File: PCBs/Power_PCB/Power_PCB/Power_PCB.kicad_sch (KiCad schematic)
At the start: 8 parts, among them IC1 ADS1115BQDGSRQ1, IC2 ADS1115BQDGSRQ1, IC3 ACS712ELCTR-20A-T, J1 XT60PW-F, J2 XT60PW-F, J3 XT60PW-F, J4 XT60PW-F, U1 ESP32-S3

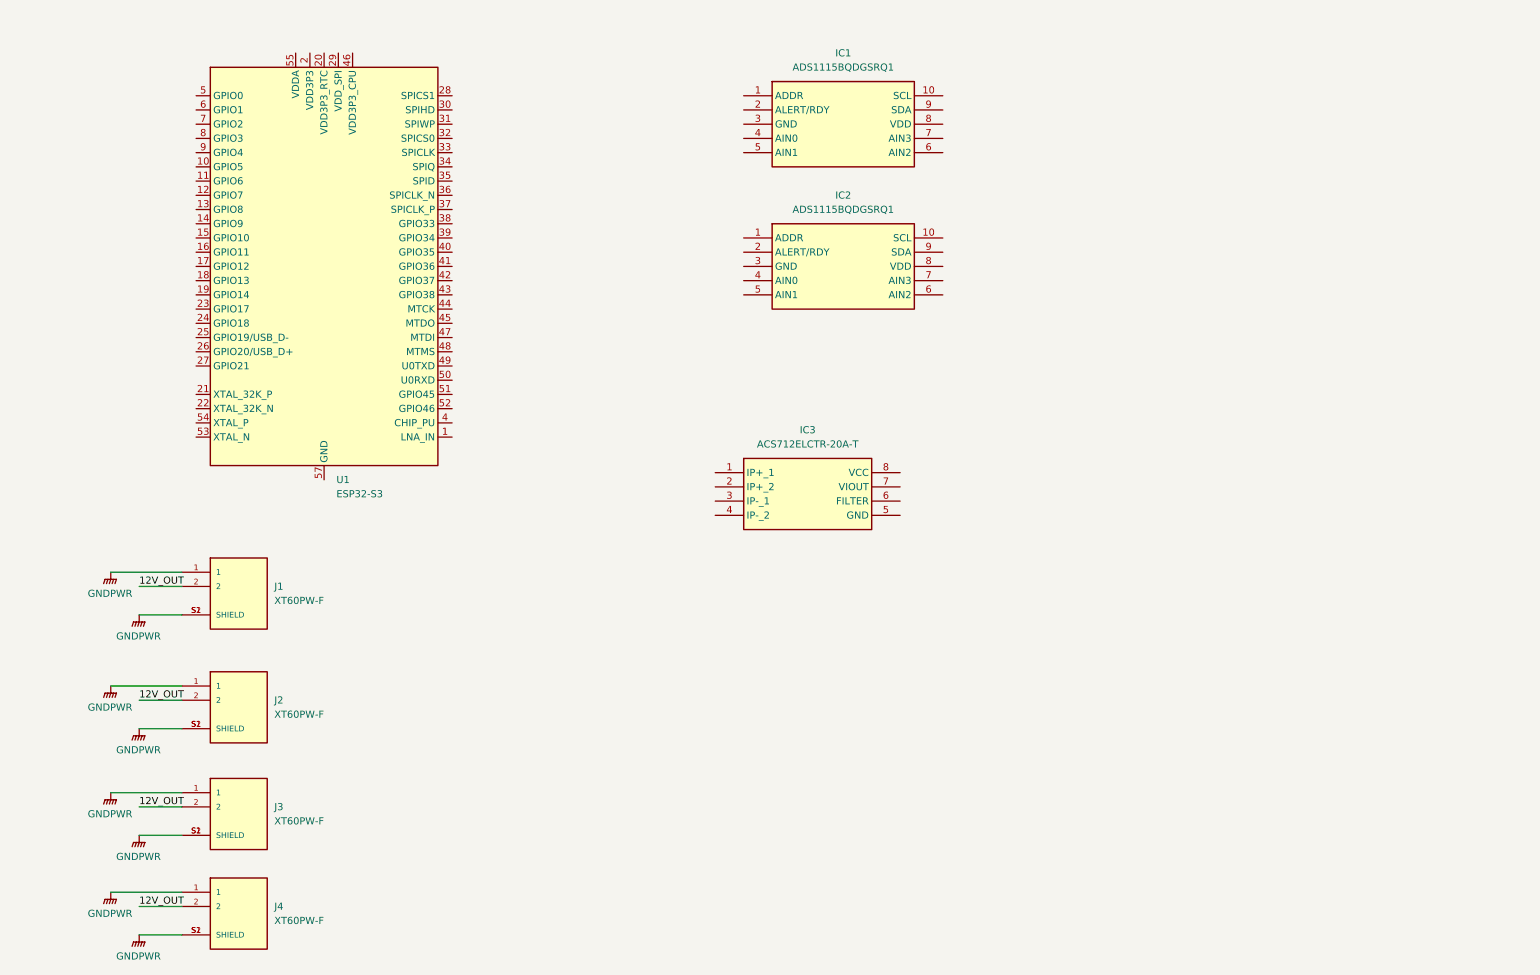
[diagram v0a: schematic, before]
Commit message: Completed power board
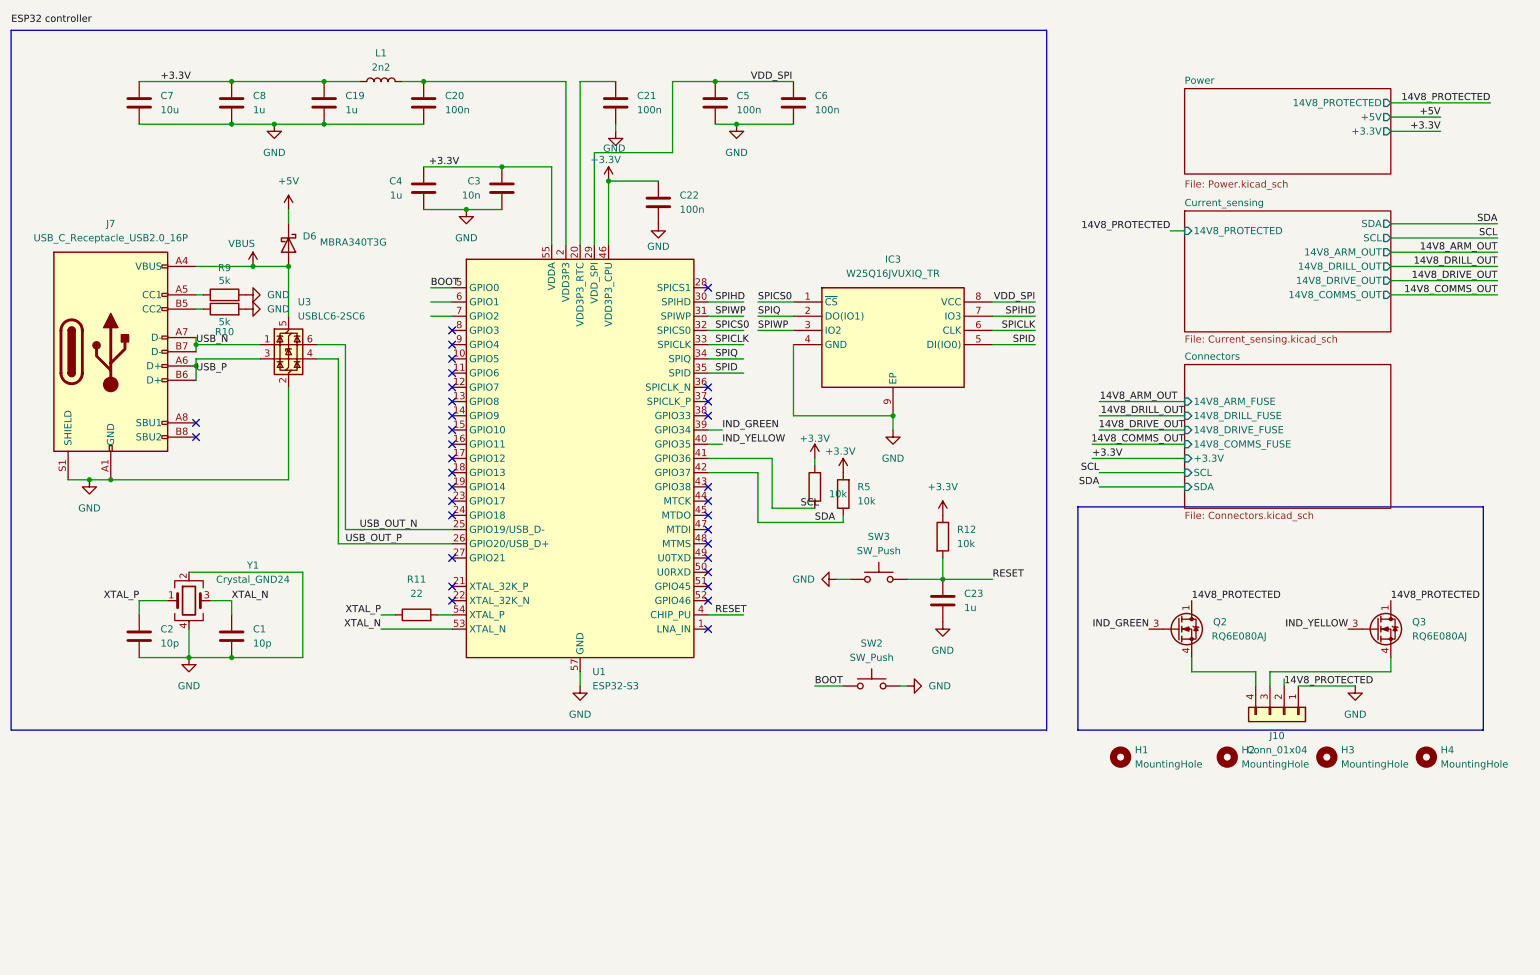
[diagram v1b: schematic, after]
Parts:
- removed IC1, IC2: ADS1115BQDGSRQ1, iprl_footprints:SOP50P490X110-10N, symbol ADS1115BQDGSRQ1:ADS1115BQDGSRQ1
- removed IC3: ACS712ELCTR-20A-T, iprl_footprints:SOIC127P600X175-8N, symbol ACS712ELCTR-20A:ACS712ELCTR-20A-T
- removed J1, J2, J3, J4: XT60PW-F, iprl_footprints:XT60PW-F:AMASS_XT60PW-F, symbol XT60PW-F:XT60PW-F
- added C1, C2: 10p, Capacitor_SMD:C_0805_2012Metric, symbol Device:C
- added C19, C23, C4, C8: 1u, Capacitor_SMD:C_0805_2012Metric, symbol Device:C
- added C20, C21, C22, C5, C6: 100n, Capacitor_SMD:C_0805_2012Metric, symbol Device:C
- added C3: 10n, Capacitor_SMD:C_0805_2012Metric, symbol Device:C
- added C7: 10u, Capacitor_SMD:C_0805_2012Metric, symbol Device:C
- added D6: MBRA340T3G, Diode_SMD:D_SMA, symbol Device:D_Schottky
- added H1, H2, H3, H4: MountingHole, MountingHole:MountingHole_3.2mm_M3, symbol Mechanical:MountingHole
- added IC3: W25Q16JVUXIQ_TR, footprints:SON50P300X200X60-9N, symbol W25Q16JVUXIQ_TR:W25Q16JVUXIQ_TR
- added J10: Conn_01x04, TerminalBlock:TerminalBlock_Altech_AK300-4_P5.00mm, symbol Connector_Generic:Conn_01x04
- added J7: USB_C_Receptacle_USB2.0_16P, iprl_footprints:TYPE-C-31-M-12, symbol Connector:USB_C_Receptacle_USB2.0_16P
- added L1: 2n2, Inductor_SMD:L_0805_2012Metric, symbol Device:L
- added Q2, Q3: RQ6E080AJ, Package_TO_SOT_SMD:TSOT-23-6, symbol Transistor_FET:RQ6E080AJ
- added R10, R9: 5k, Resistor_SMD:R_0805_2012Metric, symbol Device:R
- added R11: 22, Resistor_SMD:R_0805_2012Metric, symbol Device:R
- added R12, R5, R6: 10k, Resistor_SMD:R_0805_2012Metric, symbol Device:R
- added SW2, SW3: SW_Push, Button_Switch_SMD:SW_Push_1P1T_NO_CK_KSC6xxJ, symbol Switch:SW_Push
- added U3: USBLC6-2SC6, Package_TO_SOT_SMD:SOT-23-6, symbol Power_Protection:USBLC6-2SC6
- added Y1: Crystal_GND24, Crystal:Crystal_SMD_SeikoEpson_FA238-4Pin_3.2x2.5mm, symbol Device:Crystal_GND24
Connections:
- net at U1.2 (VDD3P3), U1.3 (VDD3P3): now also C20.1, L1.2
- net at U1.20 (VDD3P3_RTC): now also C21.1
- net USB_OUT_N: now reaches U1.25 (GPIO19/USB_D-)
- net USB_OUT_N: now also U3.6 (I/O1)
- net USB_OUT_P: now reaches U1.26 (GPIO20/USB_D+)
- net USB_OUT_P: now also U3.4 (I/O2)
- net VDD_SPI: now reaches U1.29 (VDD_SPI)
- net VDD_SPI: now also C5.1, C6.1, IC3.8 (VCC)
- net SPIHD: now reaches U1.30 (SPIHD)
- net SPIHD: now also IC3.7 (IO3)
- net SPIWP: now reaches U1.31 (SPIWP)
- net SPIWP: now also IC3.3 (IO2)
- net SPICS0: now reaches U1.32 (SPICS0)
- net SPICS0: now also IC3.1 (~{CS})
- net SPICLK: now reaches U1.33 (SPICLK)
- net SPICLK: now also IC3.6 (CLK)
- net SPIQ: now reaches U1.34 (SPIQ)
- net SPIQ: now also IC3.2 (DO(IO1))
- net SPID: now reaches U1.35 (SPID)
- net SPID: now also IC3.5 (DI(IO0))
- net IND_GREEN: now reaches U1.39 (GPIO34)
- net IND_GREEN: now also Q2.3 (G)
- net RESET: now reaches U1.4 (CHIP_PU)
- net RESET: now also C23.1, R12.2, SW3.2
- net IND_YELLOW: now reaches U1.40 (GPIO35)
- net IND_YELLOW: now also Q3.3 (G)
- net SCL: now reaches U1.41 (GPIO36)
- net SCL: now also R6.1
- net SDA: now reaches U1.42 (GPIO37)
- net SDA: now also R5.1
- net +3.3V: now reaches U1.46 (VDD3P3_CPU)
- net +3.3V: now also U1.55 (VDDA), U1.56 (VDDA), C19.1, C22.1, C3.1, C4.1, C7.1, C8.1, L1.1, R12.1, R5.2, R6.2
- net BOOT: now reaches U1.5 (GPIO0)
- net BOOT: now also SW2.1
- net XTAL_N: now reaches U1.53 (XTAL_N)
- net XTAL_N: now also C1.1, Y1.3
- net at U1.54 (XTAL_P): now also R11.2
- net GND: now reaches U1.57 (GND)
- net GND: now also C1.2, C19.2, C2.2, C20.2, C21.2, C22.2, C23.2, C3.2, C4.2, C5.2, C6.2, C7.2, C8.2, IC3.4 (GND), IC3.9 (EP), J10.1 (Pin_1), J7.A1 (GND), J7.A12 (GND), J7.B1 (GND), J7.B12 (GND), J7.S1 (SHIELD), R10.2, R9.2, SW2.2, SW3.1, U3.2 (GND), Y1.2, Y1.4
- new net: J10.3 (Pin_3), Q3.4 (S)
- new net: J10.4 (Pin_4), Q2.4 (S)
- new net: J7.B5 (CC2), R10.1
- new net: J7.A5 (CC1), R9.1
- new net +5V: D6.1 (K)
- new net 14V8_PROTECTED: J10.2 (Pin_2), Q2.1 (D), Q2.2 (D), Q2.5 (D), Q2.6 (D), Q3.1 (D), Q3.2 (D), Q3.5 (D), Q3.6 (D)
- new net USB_N: J7.A7 (D-), J7.B7 (D-), U3.1 (I/O1)
- new net USB_P: J7.A6 (D+), J7.B6 (D+), U3.3 (I/O2)
- new net VBUS: D6.2 (A), J7.A4 (VBUS), J7.A9 (VBUS), J7.B4 (VBUS), J7.B9 (VBUS), U3.5 (VBUS)
- new net XTAL_P: C2.1, R11.1, Y1.1
- no-connect marks 0 -> 33
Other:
- added sheet Connectors (Connectors.kicad_sch)
- added sheet Current_sensing (Current_sensing.kicad_sch)
- added sheet Power (Power.kicad_sch)
- moved on the sheet: U1

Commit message: Second iteration power board
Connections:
- net 14V8_PROTECTED: now also J10.3 (Pin_3); no longer J10.2 (Pin_2), Q2.1 (D), Q2.2 (D), Q2.5 (D), Q2.6 (D), Q3.1 (D), Q3.2 (D), Q3.5 (D), Q3.6 (D)
- net GND: now also J10.4 (Pin_4), Q2.4 (S), Q3.4 (S); no longer J10.1 (Pin_1)
- new net: J10.1 (Pin_1), Q3.1 (D), Q3.2 (D), Q3.5 (D), Q3.6 (D)
- new net: J10.2 (Pin_2), Q2.1 (D), Q2.2 (D), Q2.5 (D), Q2.6 (D)

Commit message: Changes from meeting
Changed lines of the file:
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@@
 (kicad_sch
-	(version 20231120)
+	(version 20250114)
 	(generator "eeschema")
-	(generator_version "8.0")
+	(generator_version "9.0")
 	(paper "A4")
+	(rectangle
+		(start 16.51 28.956)
+		(end 201.422 153.924)
+		(stroke
+			(width 0)
+			(type default)
+		)
+		(fill
+			(type none)
+		)
+	)
+	(rectangle
+		(start 207.01 114.046)
+		(end 279.4 153.924)
+		(stroke
+			(width 0)
+			(type default)
+		)
+		(fill
+			(type none)
+		)
+	)
+	(text_box "One light indicates power is present (pin 4)"
+		(exclude_from_sim no)
+		(at 231.14 121.92 0)
+		(size 25.4 7.62)
+		(margins 0.9525 0.9525 0.9525 0.9525)
+		(stroke
+			(width 0)
+			(type solid)
+		)
+		(fill
+			(type none)
+		)
+		(effects
+			(font
+				(size 1.27 1.27)
+			)
+			(justify left top)
+		)
+	)
 	(junction
 		(at 72.39 45.72)
@@
 		)
 	)
-	(rectangle
-		(start 16.51 28.956)
-		(end 201.422 153.924)
-		(stroke
-			(width 0)
-			(type default)
-		)
-		(fill
-			(type none)
-		)
-	)
-	(rectangle
-		(start 207.01 114.046)
-		(end 279.4 153.924)
-		(stroke
-			(width 0)
-			(type default)
-		)
-		(fill
-			(type none)
-		)
-	)
 	(label "SCL"
 		(at 157.48 114.3 0)
@@
 		(at 226.06 39.37)
 		(size 36.83 15.24)
+		(exclude_from_sim no)
+		(in_bom yes)
+		(on_board yes)
+		(dnp no)
 		(fields_autoplaced yes)
 		(stroke
@@
 		(at 226.06 88.646)
 		(size 36.83 25.654)
+		(exclude_from_sim no)
+		(in_bom yes)
+		(on_board yes)
+		(dnp no)
 		(fields_autoplaced yes)
 		(stroke
@@
 		(at 226.06 61.214)
 		(size 36.83 21.59)
+		(exclude_from_sim no)
+		(in_bom yes)
+		(on_board yes)
+		(dnp no)
 		(fields_autoplaced yes)
 		(stroke
@@
 		)
 	)
+	(embedded_fonts no)
 )
